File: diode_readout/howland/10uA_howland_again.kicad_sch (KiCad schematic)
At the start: 16 parts

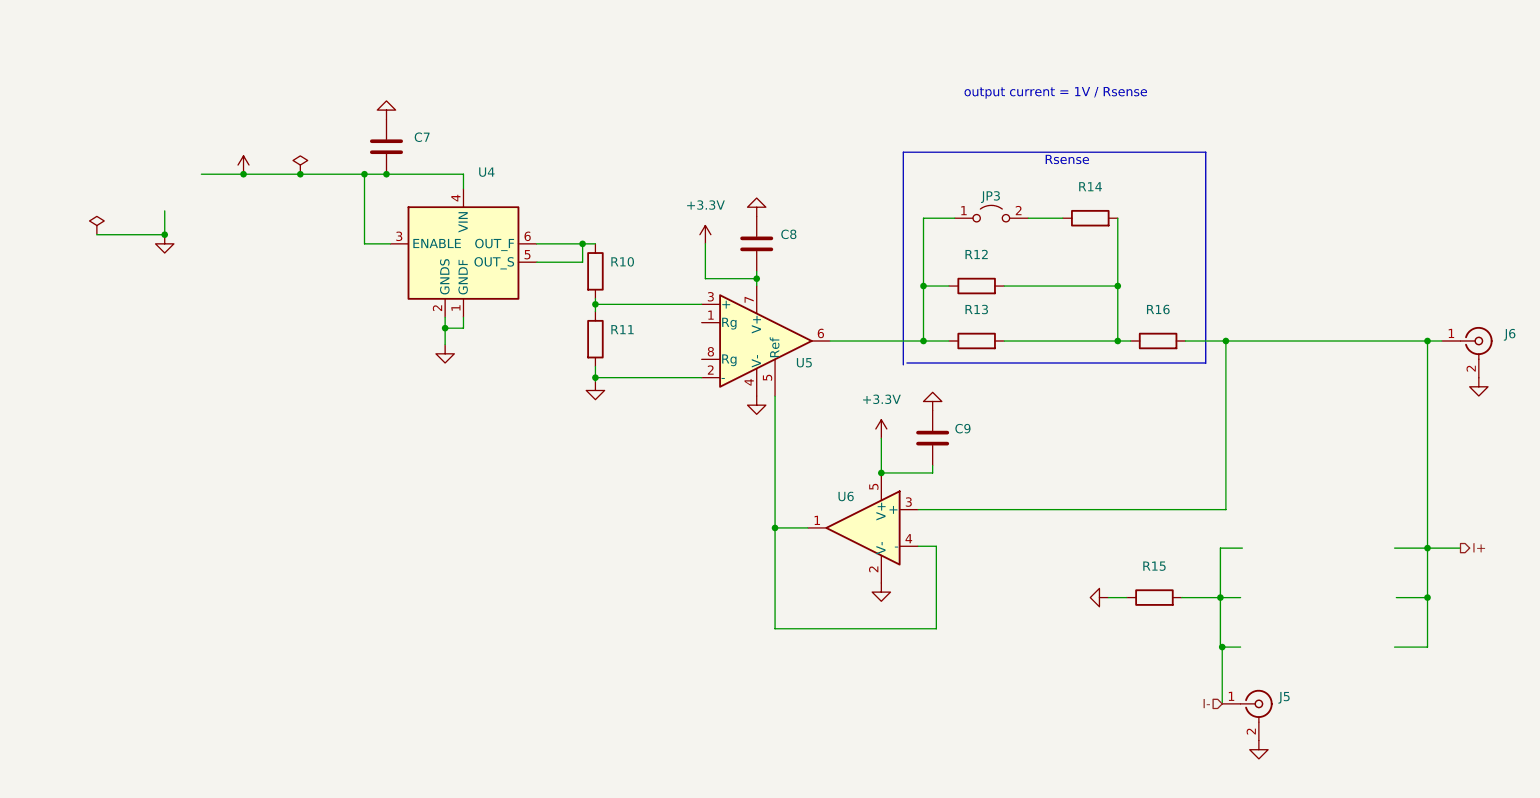
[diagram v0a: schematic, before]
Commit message: add sq_lockin_v8 and tweaks to howland diode_readout
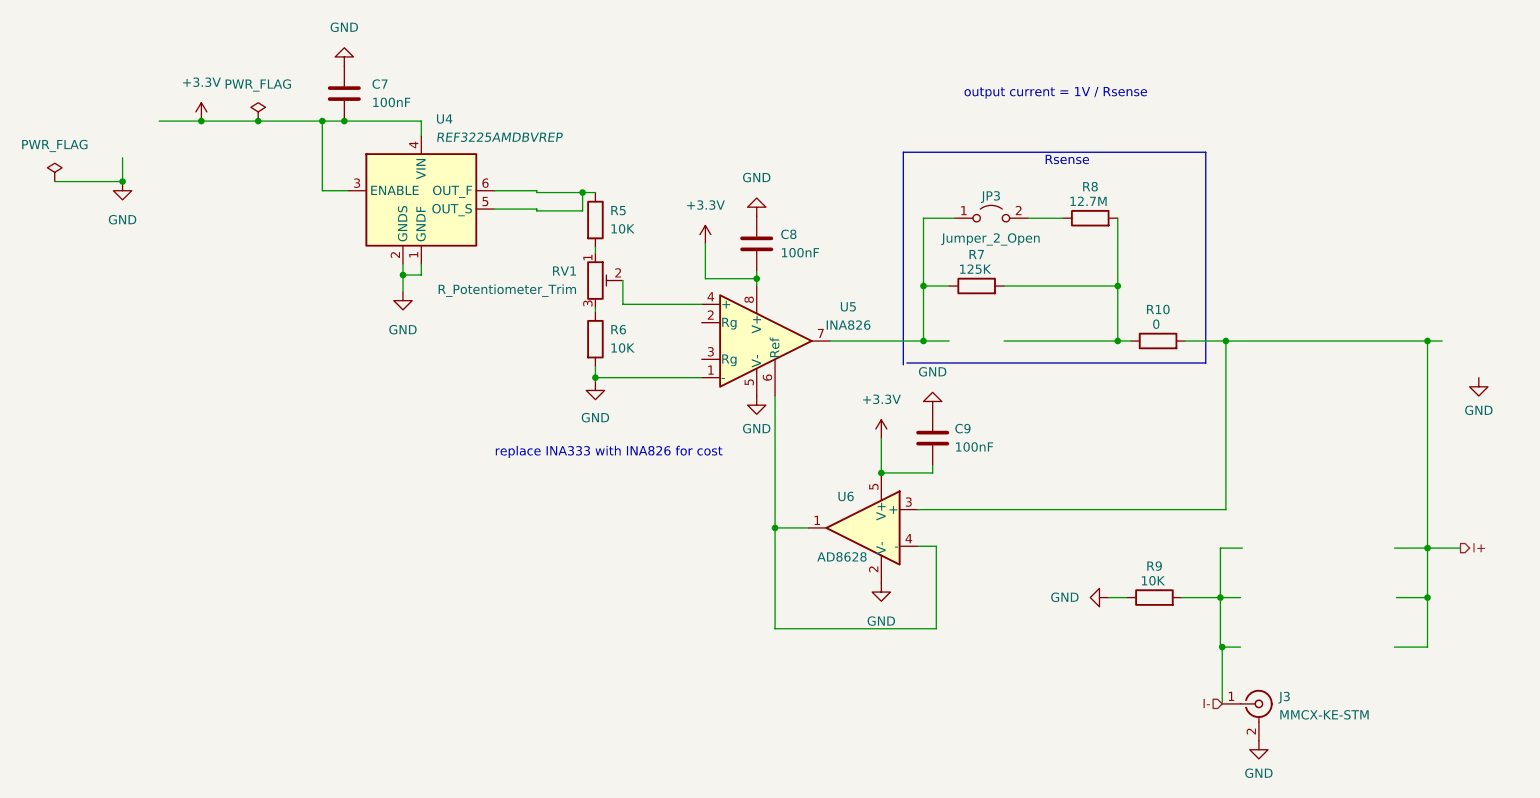
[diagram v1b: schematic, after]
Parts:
- removed J6: (no value), symbol 0JLC-6:MMCX-KE-STM
- removed R13: (no value), symbol 0JLC-6:1K
- removed U5: (no value), symbol Amplifier_Instrumentation:INA333xxDGK
- added RV1: R_Potentiometer_Trim, Potentiometer_THT:Potentiometer_Bourns_3266W_Vertical, symbol Device:R_Potentiometer_Trim
- added U5: INA826, Package_SO:SOIC-8_3.9x4.9mm_P1.27mm, symbol 0JLC-6:INA826
- C7, C8, C9: value (none) -> 100nF; footprint (none) -> Capacitor_SMD:C_0603_1608Metric_Pad1.08x0.95mm_HandSolder
- J3: renamed from J5; value (none) -> MMCX-KE-STM; footprint (none) -> 0my_footprints6:MMCX-SMD_KH-MMCX-KE-STM
- JP3: value (none) -> Jumper_2_Open; footprint (none) -> Jumper:SolderJumper-2_P1.3mm_Open_RoundedPad1.0x1.5mm
- R10: renamed from R16; value (none) -> 0; footprint (none) -> Resistor_SMD:R_0603_1608Metric_Pad0.98x0.95mm_HandSolder
- R5: renamed from R10; value (none) -> 10K; footprint (none) -> Resistor_SMD:R_0805_2012Metric; LCSC C2692723 -> C706400
- R6: renamed from R11; value (none) -> 10K; footprint (none) -> Resistor_SMD:R_0805_2012Metric; LCSC C2692723 -> C706400
- R7: renamed from R12; value (none) -> 125K; footprint (none) -> Resistor_SMD:R_0805_2012Metric
- R8: renamed from R14; value (none) -> 12.7M; footprint (none) -> Resistor_SMD:R_0805_2012Metric
- R9: renamed from R15; value (none) -> 10K; footprint (none) -> Resistor_SMD:R_0805_2012Metric
- U4: value (none) -> REF3225AMDBVREP; footprint (none) -> Package_TO_SOT_SMD:SOT-23-6
- U6: value (none) -> AD8628; footprint (none) -> Package_TO_SOT_SMD:TSOT-23-5
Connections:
- net +3V3: now also U5.8 (V+)
- net GND: now also U5.1 (-), U5.5 (V-)
- net at U6.1, U6.4 (-): now also U5.6 (Ref)
- net at R5.2: now also RV1.1; no longer R6.1
- net at JP3.1 (A), R7.1: now also U5.7
- new net: RV1.2, U5.4 (+)
- new net: R6.1, RV1.3
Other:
- note added: "replace INA333 with INA826 for cost"
- moved on the sheet: C7, R5, U4

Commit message: Commit changes to howland current source diode readout: 1.  Add 1Mohm shorts bettern V+ and I+  as well as V- and I- to mimic      this will mimic the two wire readout behaviour when the diode gets      disconnected. 2.  Add FRAM chip, 512kbits or 64kBytes of memory
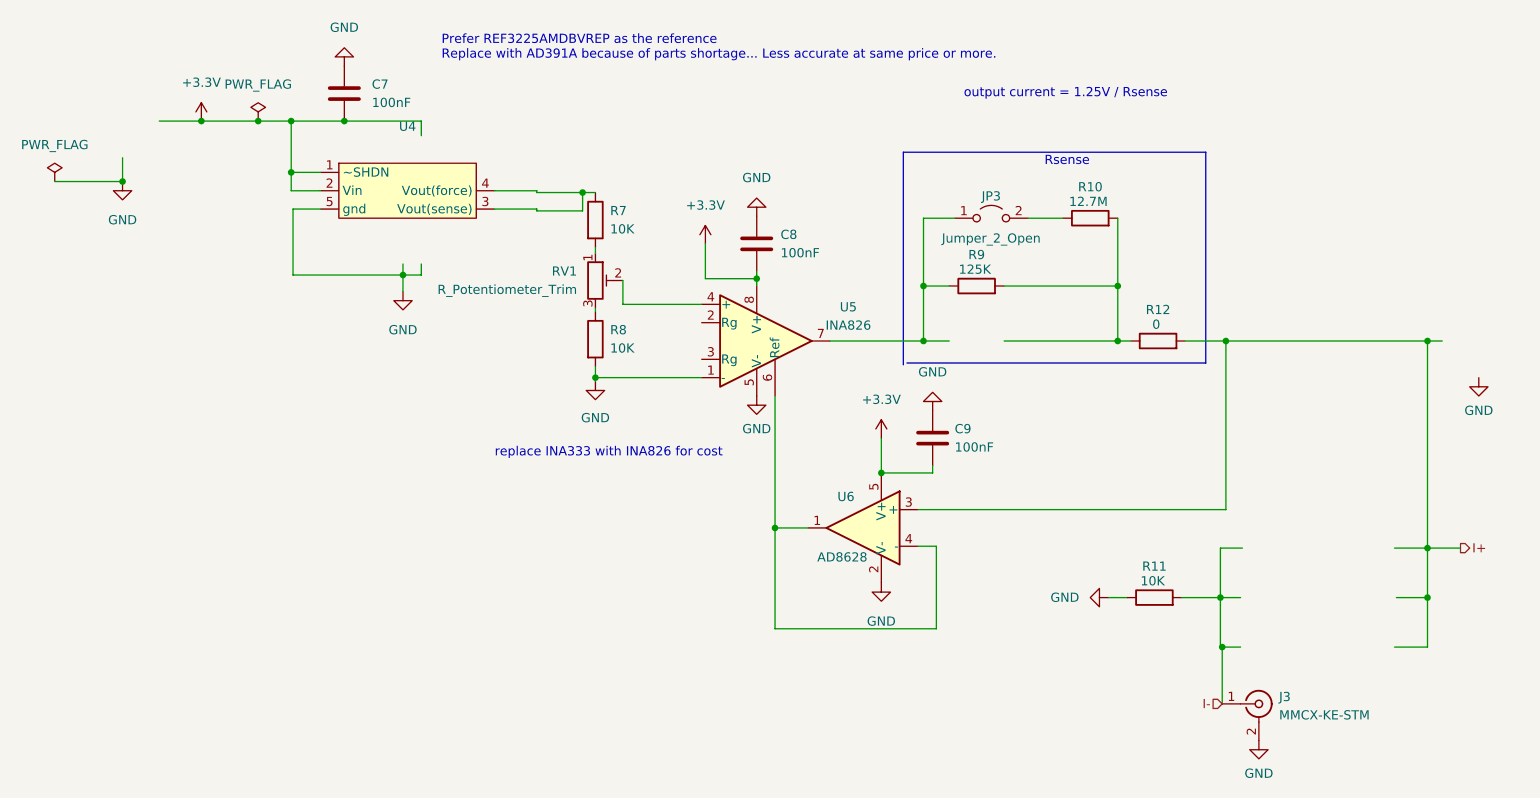
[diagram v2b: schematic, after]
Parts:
- removed U4: REF3225AMDBVREP, Package_TO_SOT_SMD:SOT-23-6, symbol Reference_Voltage:REF3225AMDBVREP
- added U4: (no value), symbol 0JLC-6:ADR391
- renumbered R8 to R10, R9 to R11, R10 to R12, R5 to R7, R6 to R8, R7 to R9
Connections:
- net +3V3: now also U4.1 (~SHDN), U4.2 (Vin)
- net GND: now also U4.5 (gnd)
- net at R7.1: now also U4.3 (Vout(sense)), U4.4 (Vout(force))
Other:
- note added: "Prefer REF3225AMDBVREP as the reference Replace with AD391A because of parts shortage... Less accurate at same price or more."
- note added: "output current = 1.25V / Rsense"
- note removed: "output current = 1V / Rsense"
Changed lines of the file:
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@@
   (junction (at 132.08 75.692) (diameter 0) (color 0 0 0 0)
   )
+  (junction (at 197.104 84.328) (diameter 0) (color 0 0 0 0)
+  )
+  (junction (at 109.728 89.408) (diameter 0) (color 0 0 0 0)
+  )
+  (junction (at 74.93 53.848) (diameter 0) (color 0 0 0 0)
+  )
+  (junction (at 196.596 126.746) (diameter 0) (color 0 0 0 0)
+  )
+  (junction (at 155.194 76.708) (diameter 0) (color 0 0 0 0)
+  )
+  (junction (at 225.044 113.03) (diameter 0) (color 0 0 0 0)
+  )
+  (junction (at 62.992 53.848) (diameter 0) (color 0 0 0 0)
+  )
   (junction (at 83.058 75.184) (diameter 0) (color 0 0 0 0)
   )
-  (junction (at 197.104 84.328) (diameter 0) (color 0 0 0 0)
-  )
-  (junction (at 109.728 89.408) (diameter 0) (color 0 0 0 0)
-  )
-  (junction (at 74.93 53.848) (diameter 0) (color 0 0 0 0)
-  )
-  (junction (at 196.596 126.746) (diameter 0) (color 0 0 0 0)
-  )
-  (junction (at 155.194 76.708) (diameter 0) (color 0 0 0 0)
-  )
-  (junction (at 225.044 113.03) (diameter 0) (color 0 0 0 0)
-  )
-  (junction (at 62.992 53.848) (diameter 0) (color 0 0 0 0)
-  )
   (junction (at 225.044 84.328) (diameter 0) (color 0 0 0 0)
   )
   (junction (at 134.62 110.236) (diameter 0) (color 0 0 0 0)
   )
-  (junction (at 71.882 53.848) (diameter 0) (color 0 0 0 0)
+  (junction (at 67.564 53.848) (diameter 0) (color 0 0 0 0)
   )
   (junction (at 155.194 84.328) (diameter 0) (color 0 0 0 0)
@@
   (junction (at 225.044 119.888) (diameter 0) (color 0 0 0 0)
   )
+  (junction (at 67.564 60.96) (diameter 0) (color 0 0 0 0)
+  )
   (junction (at 196.342 119.888) (diameter 0) (color 0 0 0 0)
   )
   (junction (at 182.118 84.328) (diameter 0) (color 0 0 0 0)
   )
+  (wire (pts (xy 83.058 75.184) (xy 83.058 77.47))
+    (stroke (width 0) (type default) (color 0 0 0 0))
+  )
   (wire (pts (xy 34.798 62.23) (xy 44.196 62.23))
     (stroke (width 0) (type default) (color 0 0 0 0))
@@
     (stroke (width 0) (type default) (color 0 0 0 0))
   )
+  (wire (pts (xy 67.564 60.96) (xy 71.628 60.96))
+    (stroke (width 0) (type default) (color 0 0 0 0))
+  )
   (wire (pts (xy 196.596 126.746) (xy 196.596 134.62))
     (stroke (width 0) (type default) (color 0 0 0 0))
@@
     (stroke (width 0) (type default) (color 0 0 0 0))
   )
+  (wire (pts (xy 67.564 53.848) (xy 74.93 53.848))
+    (stroke (width 0) (type default) (color 0 0 0 0))
+  )
   (wire (pts (xy 154.432 112.776) (xy 156.972 112.776))
     (stroke (width 0) (type default) (color 0 0 0 0))
   )
+  (wire (pts (xy 67.818 66.04) (xy 67.818 75.184))
+    (stroke (width 0) (type default) (color 0 0 0 0))
+  )
   (wire (pts (xy 191.516 84.328) (xy 197.104 84.328))
     (stroke (width 0) (type default) (color 0 0 0 0))
   )
+  (wire (pts (xy 83.058 75.184) (xy 67.818 75.184))
+    (stroke (width 0) (type default) (color 0 0 0 0))
+  )
   (wire (pts (xy 196.342 126.746) (xy 196.342 119.888))
     (stroke (width 0) (type default) (color 0 0 0 0))
   )
-  (wire (pts (xy 71.882 63.5) (xy 71.882 53.848))
-    (stroke (width 0) (type default) (color 0 0 0 0))
-  )
   (wire (pts (xy 109.728 79.756) (xy 109.728 80.264))
     (stroke (width 0) (type default) (color 0 0 0 0))
@@
     (stroke (width 0) (type default) (color 0 0 0 0))
   )
+  (wire (pts (xy 67.564 63.5) (xy 71.628 63.5))
+    (stroke (width 0) (type default) (color 0 0 0 0))
+  )
   (polyline (pts (xy 194.31 58.166) (xy 152.4 58.166))
     (stroke (width 0) (type default) (color 0 0 0 0))
@@
     (stroke (width 0) (type default) (color 0 0 0 0))
   )
-  (wire (pts (xy 71.882 53.848) (xy 74.93 53.848))
-    (stroke (width 0) (type default) (color 0 0 0 0))
-  )
   (wire (pts (xy 155.194 76.708) (xy 155.194 84.328))
     (stroke (width 0) (type default) (color 0 0 0 0))
@@
     (stroke (width 0) (type default) (color 0 0 0 0))
   )
-  (wire (pts (xy 62.992 53.848) (xy 71.882 53.848))
+  (wire (pts (xy 62.992 53.848) (xy 67.564 53.848))
+    (stroke (width 0) (type default) (color 0 0 0 0))
+  )
+  (wire (pts (xy 71.628 66.04) (xy 67.818 66.04))
     (stroke (width 0) (type default) (color 0 0 0 0))
   )
@@
     (stroke (width 0) (type default) (color 0 0 0 0))
   )
+  (wire (pts (xy 67.564 60.96) (xy 67.564 53.848))
+    (stroke (width 0) (type default) (color 0 0 0 0))
+  )
   (wire (pts (xy 95.758 63.5) (xy 101.6 63.5))
     (stroke (width 0) (type default) (color 0 0 0 0))
@@
     (stroke (width 0) (type default) (color 0 0 0 0))
   )
-  (wire (pts (xy 83.058 75.184) (xy 83.058 77.47))
+  (wire (pts (xy 83.058 73.66) (xy 83.058 75.184))
+    (stroke (width 0) (type default) (color 0 0 0 0))
+  )
+  (wire (pts (xy 67.564 63.5) (xy 67.564 60.96))
     (stroke (width 0) (type default) (color 0 0 0 0))
   )
@@
   )
   (wire (pts (xy 154.432 107.696) (xy 197.104 107.696))
-    (stroke (width 0) (type default) (color 0 0 0 0))
-  )
-  (wire (pts (xy 75.438 63.5) (xy 71.882 63.5))
-    (stroke (width 0) (type default) (color 0 0 0 0))
-  )
-  (wire (pts (xy 83.058 73.66) (xy 83.058 75.184))
     (stroke (width 0) (type default) (color 0 0 0 0))
   )
@@
     (effects (font (size 1.27 1.27)) (justify left bottom))
   )
-  (text "output current = 1V / Rsense" (at 160.782 50.8 0)
+  (text "output current = 1.25V / Rsense" (at 160.782 50.8 0)
     (effects (font (size 1.27 1.27)) (justify left bottom))
   )
@@
     (effects (font (size 1.27 1.27)) (justify left bottom))
   )
+  (text "Prefer REF3225AMDBVREP as the reference\nReplace with AD391A because of parts shortage... Less accurate at same price or more."
+    (at 88.392 45.466 0)
+    (effects (font (size 1.27 1.27)) (justify left bottom))
+  )
   (hierarchical_label "I+" (shape output) (at 229.616 113.03 0)
     (effects (font (size 1.27 1.27)) (justify left))
@@
   (symbol (lib_id "0JLC-6:1K") (at 178.308 67.31 90) (unit 1)
     (in_bom yes) (on_board yes)
-    (property "Reference" "R8" (id 0) (at 178.308 62.992 90))
+    (property "Reference" "R10" (id 0) (at 178.308 62.992 90))
     (property "Value" "12.7M" (id 1) (at 178.054 65.024 90))
     (property "Footprint" "Resistor_SMD:R_0805_2012Metric" (id 2) (at 178.308 69.088 90)
@@
     (pin "1")
     (pin "2")
+  )
+  (symbol (lib_id "0JLC-6:ADR391") (at 84.328 64.77 0) (unit 1)
+    (in_bom yes) (on_board yes) (fields_autoplaced)
+    (property "Reference" "U4" (id 0) (at 83.693 54.61 0))
+    (property "Value" "" (id 1) (at 83.693 57.15 0))
+    (property "Footprint" "" (id 2) (at 75.438 64.77 0)
+      (effects (font (size 1.27 1.27)) hide)
+    )
+    (property "Datasheet" "" (id 3) (at 75.438 64.77 0)
+      (effects (font (size 1.27 1.27)) hide)
+    )
+    (property "LCSC" "C141376" (id 4) (at 81.788 64.77 0)
+      (effects (font (size 1.27 1.27)) hide)
+    )
+    (property "MPN" "ADR391AUJZ-REEL7 " (id 5) (at 81.788 64.77 0)
+      (effects (font (size 1.27 1.27)) hide)
+    )
+    (pin "1")
+    (pin "2")
+    (pin "3")
+    (pin "4")
+    (pin "5")
   )
   (symbol (lib_id "power:+3.3V") (at 124.968 70.866 0) (unit 1)
@@
   (symbol (lib_id "0JLC-6:1K") (at 109.728 67.564 0) (unit 1)
     (in_bom yes) (on_board yes) (fields_autoplaced)
-    (property "Reference" "R5" (id 0) (at 111.76 66.2939 0)
+    (property "Reference" "R7" (id 0) (at 111.76 66.2939 0)
       (effects (font (size 1.27 1.27)) (justify left))
     )
@@
     (pin "1")
     (pin "2")
-  )
-  (symbol (lib_id "Reference_Voltage:REF3225AMDBVREP") (at 85.598 63.5 0) (unit 1)
-    (in_bom yes) (on_board yes) (fields_autoplaced)
-    (property "Reference" "U4" (id 0) (at 87.6174 53.594 0)
-      (effects (font (size 1.27 1.27)) (justify left))
-    )
-    (property "Value" "REF3225AMDBVREP" (id 1) (at 87.6174 56.134 0)
-      (effects (font (size 1.27 1.27) italic) (justify left))
-    )
-    (property "Footprint" "Package_TO_SOT_SMD:SOT-23-6" (id 2) (at 87.503 73.025 0)
-      (effects (font (size 1.27 1.27) italic) (justify left) hide)
-    )
-    (property "Datasheet" "http://www.ti.com/lit/ds/symlink/ref3240-ep.pdf" (id 3) (at 85.598 62.23 0)
-      (effects (font (size 1.27 1.27) italic) hide)
-    )
-    (pin "1")
-    (pin "2")
-    (pin "3")
-    (pin "4")
-    (pin "5")
-    (pin "6")
   )
   (symbol (lib_id "0JLC-6:1K") (at 187.198 119.888 90) (unit 1)
     (in_bom yes) (on_board yes)
-    (property "Reference" "R9" (id 0) (at 187.198 115.57 90))
+    (property "Reference" "R11" (id 0) (at 187.198 115.57 90))
     (property "Value" "10K" (id 1) (at 186.944 117.602 90))
     (property "Footprint" "Resistor_SMD:R_0805_2012Metric" (id 2) (at 187.198 121.666 90)
@@
   (symbol (lib_id "0JLC-6:1K") (at 187.706 84.328 90) (unit 1)
     (in_bom yes) (on_board yes)
-    (property "Reference" "R10" (id 0) (at 187.706 80.01 90))
+    (property "Reference" "R12" (id 0) (at 187.706 80.01 90))
     (property "Value" "0" (id 1) (at 187.452 82.042 90))
     (property "Footprint" "Resistor_SMD:R_0603_1608Metric_Pad0.98x0.95mm_HandSolder" (id 2) (at 187.706 86.106 90)
@@
   (symbol (lib_id "0JLC-6:1K") (at 162.56 76.708 90) (unit 1)
     (in_bom yes) (on_board yes)
-    (property "Reference" "R7" (id 0) (at 162.56 72.39 90))
+    (property "Reference" "R9" (id 0) (at 162.56 72.39 90))
     (property "Value" "125K" (id 1) (at 162.306 74.422 90))
     (property "Footprint" "Resistor_SMD:R_0805_2012Metric" (id 2) (at 162.56 78.486 90)
@@
   (symbol (lib_id "0JLC-6:1K") (at 109.728 84.074 0) (unit 1)
     (in_bom yes) (on_board yes) (fields_autoplaced)
-    (property "Reference" "R6" (id 0) (at 111.76 82.8039 0)
-      (effects (font (size 1.27 1.27)) (justify left))
-    )
+    (property "Reference" "R8" (id 0) (at 111.76 82.8039 0)
+      (effects (font (size 1.27 1.27)) (justify left))
+    )
